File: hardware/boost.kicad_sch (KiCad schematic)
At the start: 23 parts, among them Q1 S8550, U1 LM5158

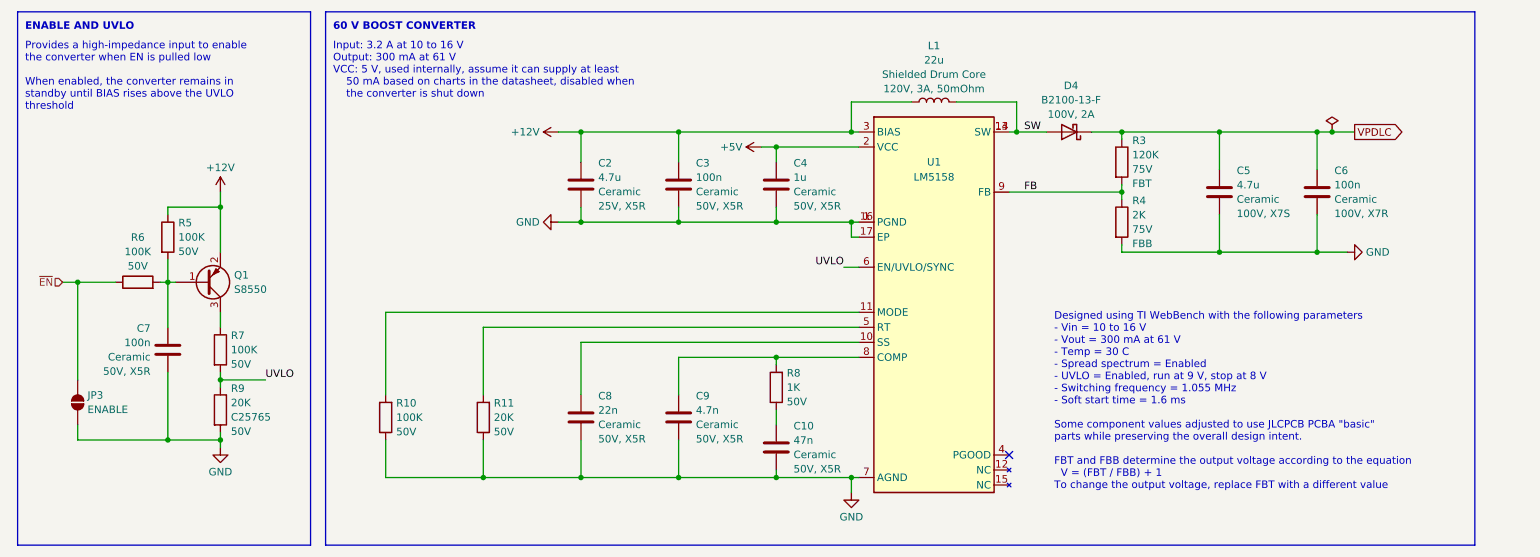
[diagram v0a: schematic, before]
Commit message: Revised layout using LM5108 and discrete FETs
LM5108 is less expensive but it requires more board area.  In lieu of
active current limiting, we rely on the LM5158 hiccup overload
protection.  The FETs are intentionally oversized to handle large
current pulses when switching the polarity of the capacitive load.

This design is complete and ready for manufacture.
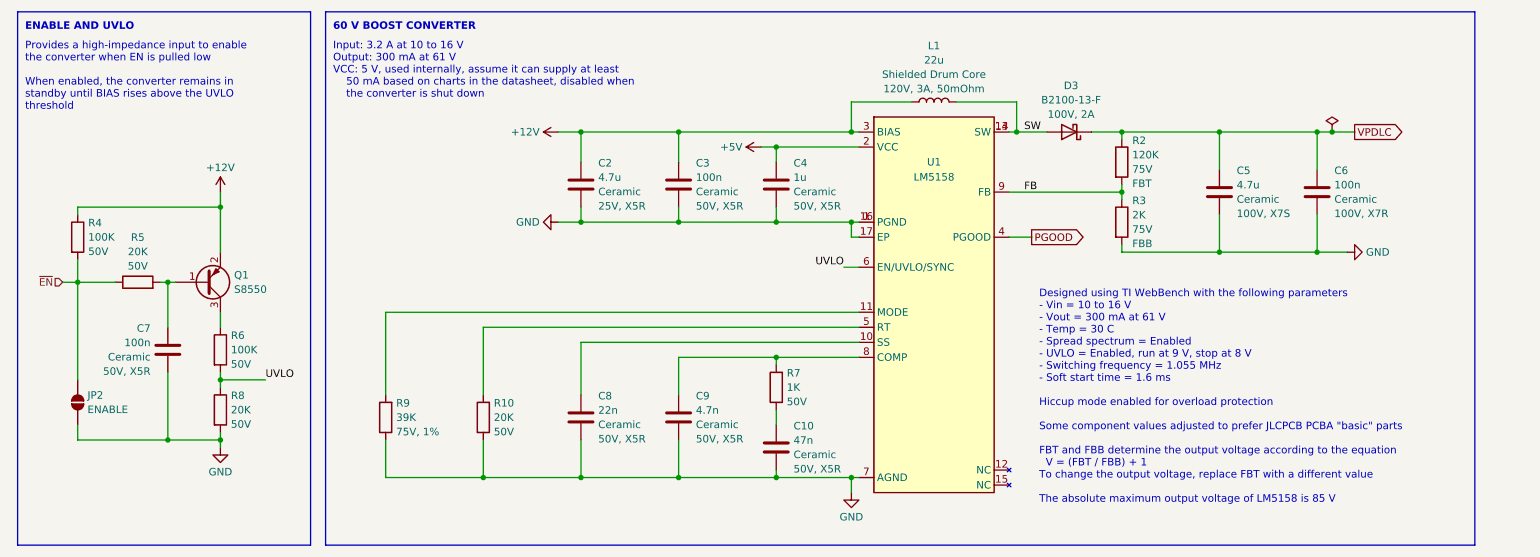
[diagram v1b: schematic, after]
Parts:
- R5: renamed from R6; value 100K -> 20K; LCSC C25741 -> C25765
- R9: renamed from R10; value 100K -> 39K; footprint Resistor_SMD:R_0402_1005Metric -> Resistor_SMD:R_0603_1608Metric; LCSC C25741 -> C23153; Rating 50V -> 75V, 1%
- U1: FT Rotation Offset (none) -> 270
- renumbered D4 to D3, JP3 to JP2, R11 to R10, R3 to R2, R4 to R3, R5 to R4, R7 to R6, R8 to R7, R9 to R8
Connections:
- net ~{EN}: now also R4.2
- net at C7.1, Q1.1 (B), R5.2: no longer R4.2
- net PGOOD: now reaches U1.4 (PGOOD)
- no-connect marks 1 -> 0
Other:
- note added: "Designed using TI WebBench with the following parameters - Vin = 10 to 16 V - Vout = 300 mA at 61 V - Temp = 30 C - Spread spectrum = Enabled - UVLO = Enabled, run at 9 V, stop at 8 V - Switching frequency = 1.055 MHz - Soft start time = 1.6 ms Hiccup mode enabled for overload protection Some component values adjusted to prefer JLCPCB PCBA "basic" parts FBT and FBB determine the output voltage ac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"
- note removed: "Designed using TI WebBench with the following parameters - Vin = 10 to 16 V - Vout = 300 mA at 61 V - Temp = 30 C - Spread spectrum = Enabled - UVLO = Enabled, run at 9 V, stop at 8 V - Switching frequency = 1.055 MHz - Soft start time = 1.6 ms Some component values adjusted to use JLCPCB PCBA "basic" parts while preserving the overall design intent. FBT and FBB determine the output voltage accor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"
- moved on the sheet: R4
